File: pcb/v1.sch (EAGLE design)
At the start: 54 parts, among them U2 MMBT3904, U3 MMBT3904, U4 MMBT3904, U5 MMBT3904

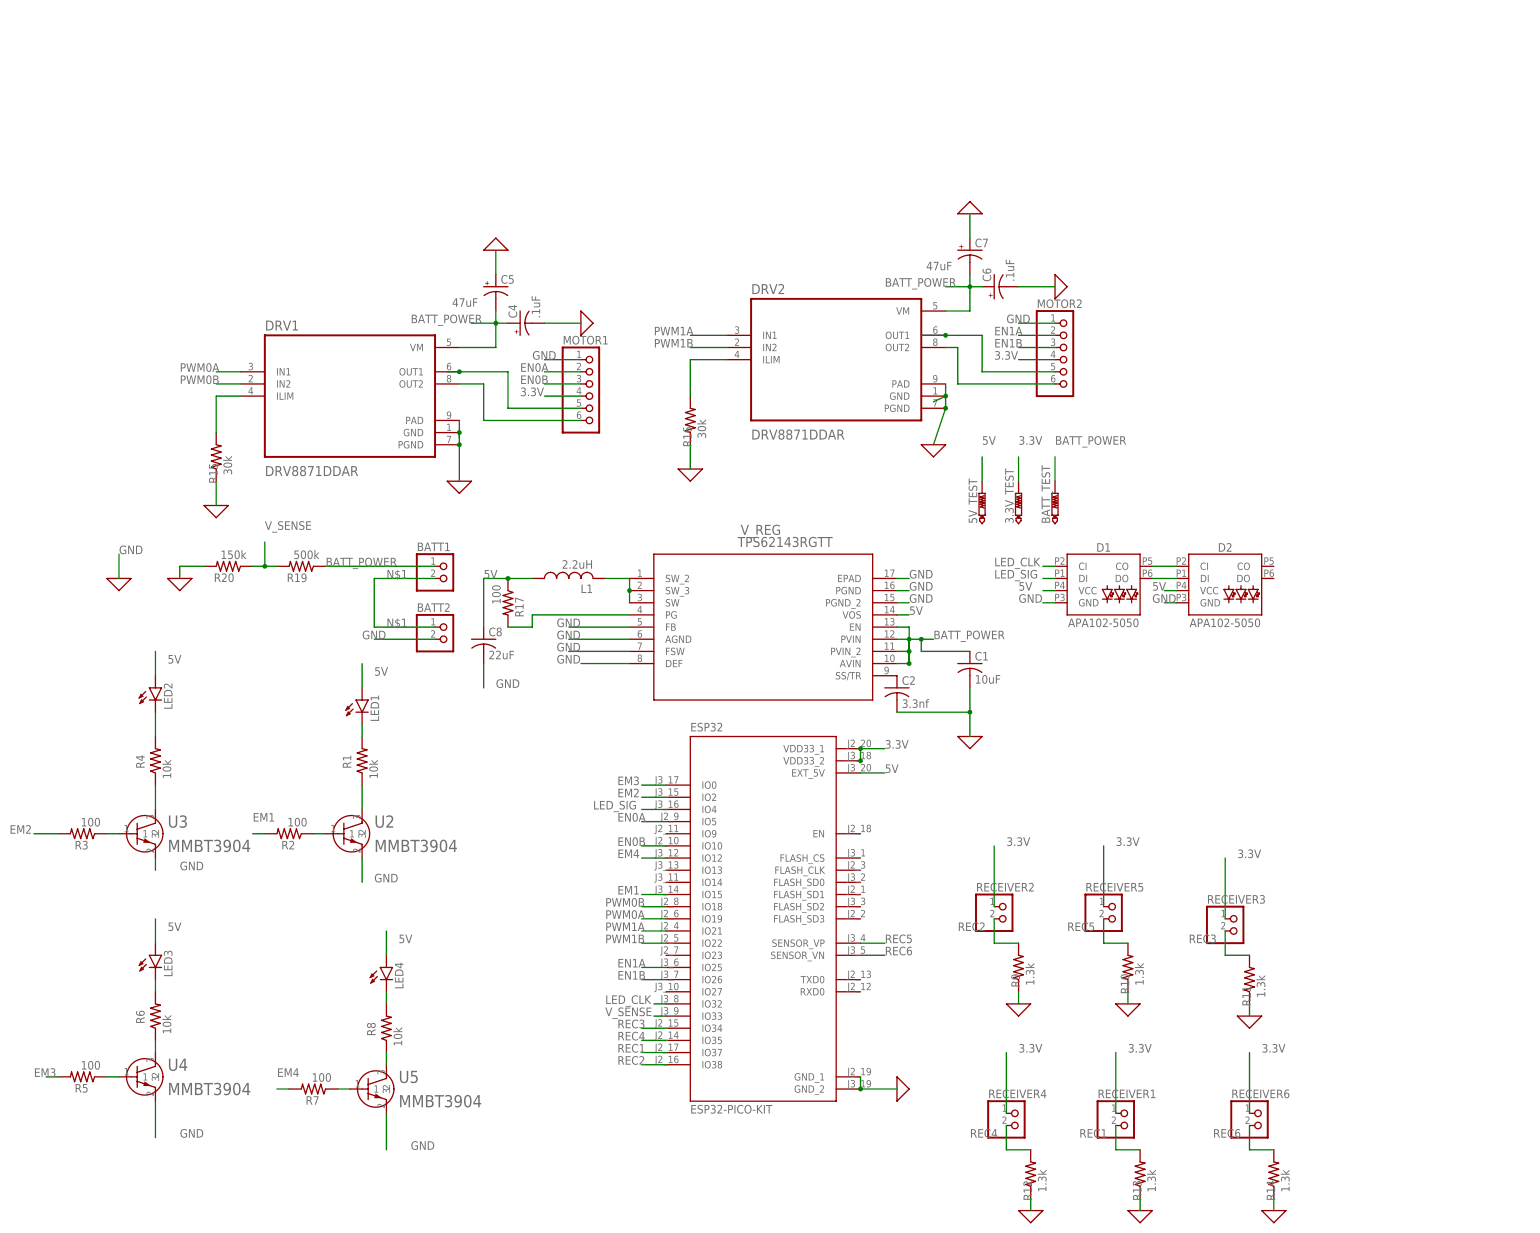
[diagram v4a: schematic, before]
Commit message: Changed the voltage regulator and updated the pcb
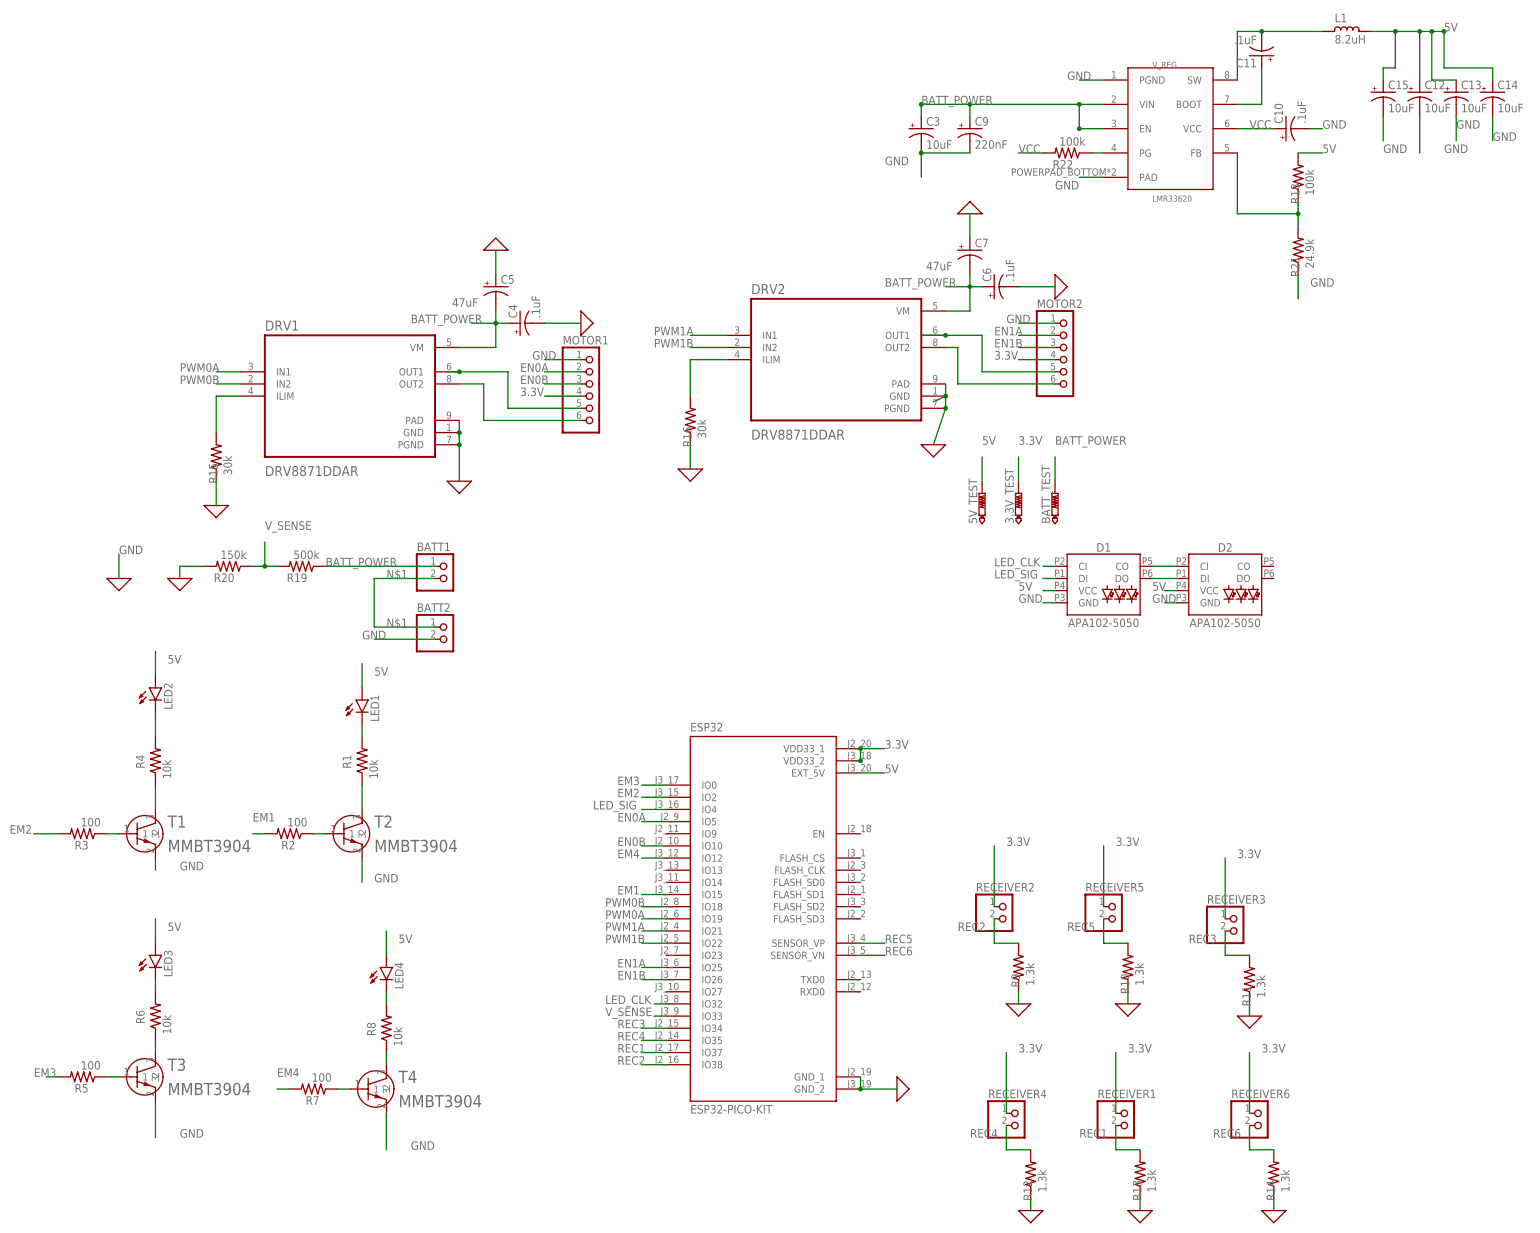
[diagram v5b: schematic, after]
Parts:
- removed C1: 10uF, rcl:C-USC1210
- removed C2: 3.3nf, rcl:C-USC1210
- removed C8: 22uF, rcl:C-USC0805
- removed R17: 100, rcl:R-US_M1206
- added C10, C11: .1uF, rcl:CPOL-USA/3216-18R
- added C12, C13, C14, C15, C3: 10uF, rcl:CPOL-USA/3216-18R
- added C9: 220nF, rcl:CPOL-USA/3216-18R
- added R18: 100k, rcl:R-US_M2012
- added R21: 24.9k, rcl:R-US_M2012
- added R22: 100k, rcl:R-US_M1206
- L1: value 2.2uH -> 8.2uH; device XFL4020:XFL4020 -> rc-master-smd:L_PM1812
- V_REG: value TPS62143RGTT -> LMR33620; device TPS61243RGTT:TPS62143RGTT -> LMR33620:LMR33620
- renumbered U2 to T2, U3 to T1, U4 to T3, U5 to T4
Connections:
- net N$4 renamed T1
- removed net N$2: C2.1, V_REG.SS/TR
- removed net N$21: L1.2, V_REG.SW, V_REG.SW_2, V_REG.SW_3
- removed net N$22: R17.2, V_REG.PG
- new net N$23: R18.1, R21.2, V_REG.FB
- new net N$25: C11.+, V_REG.BOOT
- new net N$26: C11.-, L1.2, V_REG.SW
- new net PG: R22.1, V_REG.PG
- new net VCC: C10.+, R22.2, V_REG.VCC
- net 5V: now also C12.+, C13.+, C14.+, C15.+, R18.2; no longer C8.1, R17.1, V_REG.VOS
- net BATT_POWER: now also C3.+, C9.+, V_REG.VIN; no longer C1.1, V_REG.AVIN, V_REG.PVIN, V_REG.PVIN_2
- net GND: now also C10.-, C12.-, C13.-, C14.-, C15.-, C3.-, C9.-, R21.1, V_REG.PAD; no longer C1.2, C2.2, C8.2, V_REG.AGND, V_REG.DEF, V_REG.EPAD, V_REG.FB, V_REG.FSW, V_REG.PGND_2

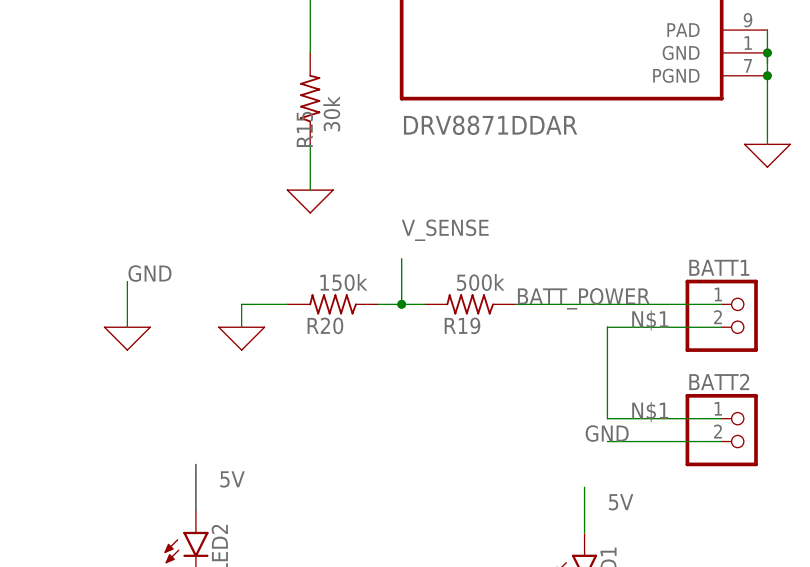
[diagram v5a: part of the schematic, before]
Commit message: Changed the resistive voltage divider values
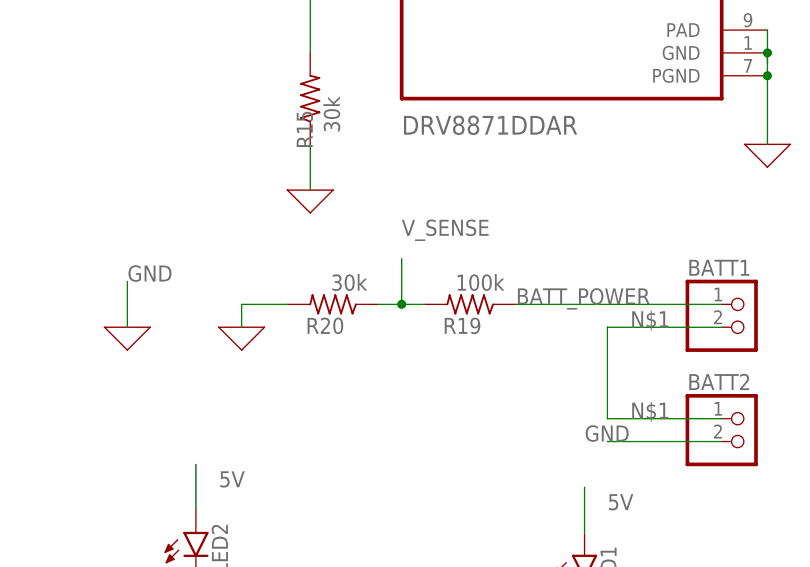
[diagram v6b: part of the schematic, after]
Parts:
- R15, R16, R18, R21: device rcl:R-US_M2012 -> rcl:R-US_M1206
- R19: value 500k -> 100k
- R20: value 150k -> 30k
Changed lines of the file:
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@@
 <part name="X_13" library="ngspice-simulation" library_urn="urn:adsk.eagle:library:527439" deviceset="GND" device=""/>
 <part name="X_14" library="ngspice-simulation" library_urn="urn:adsk.eagle:library:527439" deviceset="GND" device=""/>
-<part name="R15" library="rcl" library_urn="urn:adsk.eagle:library:334" deviceset="R-US_" device="M2012" package3d_urn="urn:adsk.eagle:package:23561/1" value="30k"/>
+<part name="R15" library="rcl" library_urn="urn:adsk.eagle:library:334" deviceset="R-US_" device="M1206" package3d_urn="urn:adsk.eagle:package:23566/1" value="30k"/>
 <part name="X_15" library="ngspice-simulation" library_urn="urn:adsk.eagle:library:527439" deviceset="GND" device=""/>
 <part name="X_16" library="ngspice-simulation" library_urn="urn:adsk.eagle:library:527439" deviceset="GND" device=""/>
@@
 <part name="X_17" library="ngspice-simulation" library_urn="urn:adsk.eagle:library:527439" deviceset="GND" device=""/>
 <part name="X_18" library="ngspice-simulation" library_urn="urn:adsk.eagle:library:527439" deviceset="GND" device=""/>
-<part name="R16" library="rcl" library_urn="urn:adsk.eagle:library:334" deviceset="R-US_" device="M2012" package3d_urn="urn:adsk.eagle:package:23561/1" value="30k"/>
+<part name="R16" library="rcl" library_urn="urn:adsk.eagle:library:334" deviceset="R-US_" device="M1206" package3d_urn="urn:adsk.eagle:package:23566/1" value="30k"/>
 <part name="X_19" library="ngspice-simulation" library_urn="urn:adsk.eagle:library:527439" deviceset="GND" device=""/>
 <part name="X_20" library="ngspice-simulation" library_urn="urn:adsk.eagle:library:527439" deviceset="GND" device=""/>
@@
 <part name="LED4" library="led" library_urn="urn:adsk.eagle:library:259" deviceset="LED" device="5MM" package3d_urn="urn:adsk.eagle:package:15799/2"/>
 <part name="R8" library="rcl" library_urn="urn:adsk.eagle:library:334" deviceset="R-US_" device="M1206" package3d_urn="urn:adsk.eagle:package:23566/1" value="10k"/>
-<part name="R19" library="rcl" library_urn="urn:adsk.eagle:library:334" deviceset="R-US_" device="M1206" package3d_urn="urn:adsk.eagle:package:23566/1" value="500k"/>
-<part name="R20" library="rcl" library_urn="urn:adsk.eagle:library:334" deviceset="R-US_" device="M1206" package3d_urn="urn:adsk.eagle:package:23566/1" value="150k"/>
+<part name="R19" library="rcl" library_urn="urn:adsk.eagle:library:334" deviceset="R-US_" device="M1206" package3d_urn="urn:adsk.eagle:package:23566/1" value="100k"/>
+<part name="R20" library="rcl" library_urn="urn:adsk.eagle:library:334" deviceset="R-US_" device="M1206" package3d_urn="urn:adsk.eagle:package:23566/1" value="30k"/>
 <part name="X_23" library="ngspice-simulation" library_urn="urn:adsk.eagle:library:527439" deviceset="GND" device=""/>
 <part name="X_22" library="ngspice-simulation" library_urn="urn:adsk.eagle:library:527439" deviceset="GND" device=""/>
@@
 <part name="C9" library="rcl" library_urn="urn:adsk.eagle:library:334" deviceset="CPOL-US" device="A/3216-18R" package3d_urn="urn:adsk.eagle:package:23410/2" value="220nF"/>
 <part name="C10" library="rcl" library_urn="urn:adsk.eagle:library:334" deviceset="CPOL-US" device="A/3216-18R" package3d_urn="urn:adsk.eagle:package:23410/2" value=".1uF"/>
-<part name="R18" library="rcl" library_urn="urn:adsk.eagle:library:334" deviceset="R-US_" device="M2012" package3d_urn="urn:adsk.eagle:package:23561/1" value="100k"/>
-<part name="R21" library="rcl" library_urn="urn:adsk.eagle:library:334" deviceset="R-US_" device="M2012" package3d_urn="urn:adsk.eagle:package:23561/1" value="24.9k"/>
+<part name="R18" library="rcl" library_urn="urn:adsk.eagle:library:334" deviceset="R-US_" device="M1206" package3d_urn="urn:adsk.eagle:package:23566/1" value="100k"/>
+<part name="R21" library="rcl" library_urn="urn:adsk.eagle:library:334" deviceset="R-US_" device="M1206" package3d_urn="urn:adsk.eagle:package:23566/1" value="24.9k"/>
 <part name="C11" library="rcl" library_urn="urn:adsk.eagle:library:334" deviceset="CPOL-US" device="A/3216-18R" package3d_urn="urn:adsk.eagle:package:23410/2" value=".1uF"/>
 <part name="C12" library="rcl" library_urn="urn:adsk.eagle:library:334" deviceset="CPOL-US" device="A/3216-18R" package3d_urn="urn:adsk.eagle:package:23410/2" value="10uF"/>

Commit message: Changed strawberry and caps. Added gerber files
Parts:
- C5, C7: device rcl:CPOL-US153CLV-0605 -> rcl:CPOL-US150CLZ-0810
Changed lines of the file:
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@@
 <part name="DRV1" library="DRV8871DDAR" deviceset="DRV8871DDAR" device=""/>
 <part name="C4" library="rcl" library_urn="urn:adsk.eagle:library:334" deviceset="CPOL-US" device="A/3216-18R" package3d_urn="urn:adsk.eagle:package:23410/2" value=".1uF"/>
-<part name="C5" library="rcl" library_urn="urn:adsk.eagle:library:334" deviceset="CPOL-US" device="153CLV-0605" package3d_urn="urn:adsk.eagle:package:23398/1" value="47uF"/>
+<part name="C5" library="rcl" library_urn="urn:adsk.eagle:library:334" deviceset="CPOL-US" device="150CLZ-0810" package3d_urn="urn:adsk.eagle:package:23394/1" value="47uF"/>
 <part name="X_13" library="ngspice-simulation" library_urn="urn:adsk.eagle:library:527439" deviceset="GND" device=""/>
 <part name="X_14" library="ngspice-simulation" library_urn="urn:adsk.eagle:library:527439" deviceset="GND" device=""/>
@@
 <part name="DRV2" library="DRV8871DDAR" deviceset="DRV8871DDAR" device=""/>
 <part name="C6" library="rcl" library_urn="urn:adsk.eagle:library:334" deviceset="CPOL-US" device="A/3216-18R" package3d_urn="urn:adsk.eagle:package:23410/2" value=".1uF"/>
-<part name="C7" library="rcl" library_urn="urn:adsk.eagle:library:334" deviceset="CPOL-US" device="153CLV-0605" package3d_urn="urn:adsk.eagle:package:23398/1" value="47uF"/>
+<part name="C7" library="rcl" library_urn="urn:adsk.eagle:library:334" deviceset="CPOL-US" device="150CLZ-0810" package3d_urn="urn:adsk.eagle:package:23394/1" value="47uF"/>
 <part name="X_17" library="ngspice-simulation" library_urn="urn:adsk.eagle:library:527439" deviceset="GND" device=""/>
 <part name="X_18" library="ngspice-simulation" library_urn="urn:adsk.eagle:library:527439" deviceset="GND" device=""/>
